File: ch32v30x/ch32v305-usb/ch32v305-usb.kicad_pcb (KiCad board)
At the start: 2 copper layers, 154 x 44 mm, 32 parts, among them J1 USB_C_Receptacle_USB2.0, J2 PGM, J3 RND, J4 JMP-PD, J5 MNT, J6 MNT, J7 MNT, SW1 KEY, SW2 KEY, SW3 KEY, SW4 KEY, SW5 KEY, SW6 KEY, SW7 KEY, SW8 KEY, U1 CH32V305FBP6, U3 3.3vReg, Y1 8MHz12pF

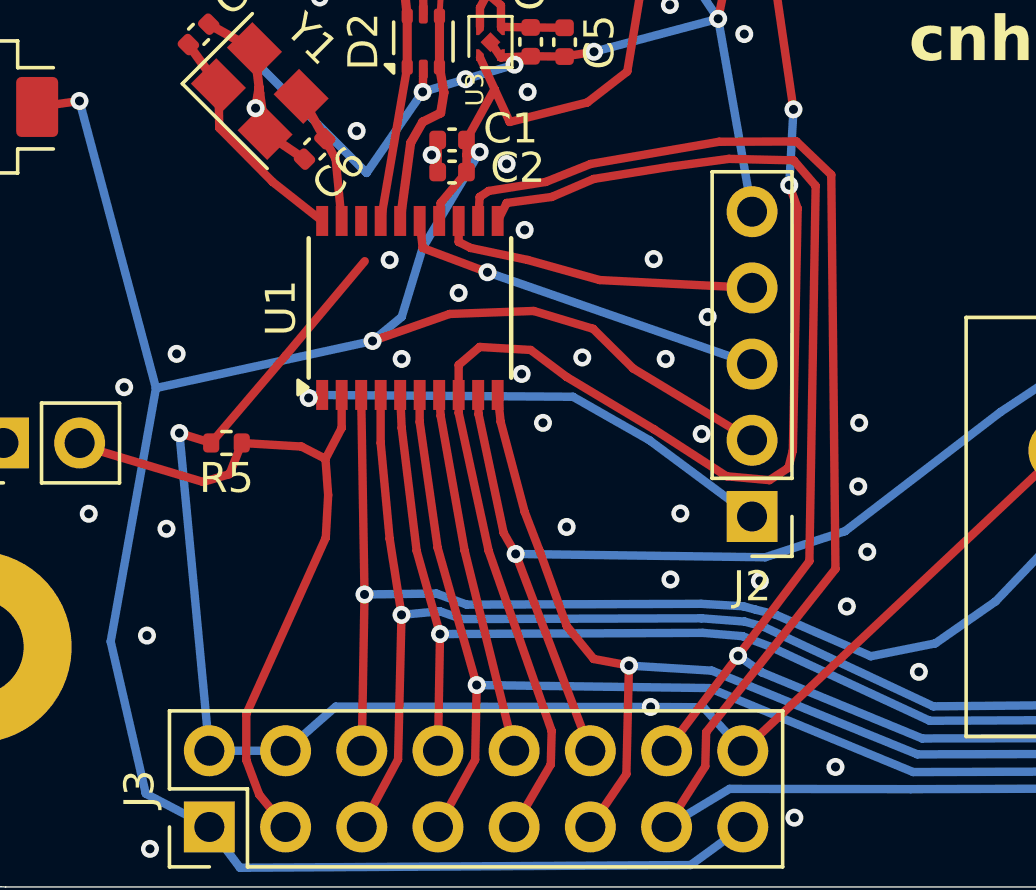
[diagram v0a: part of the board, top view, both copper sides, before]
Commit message: Tweak board to include some pins
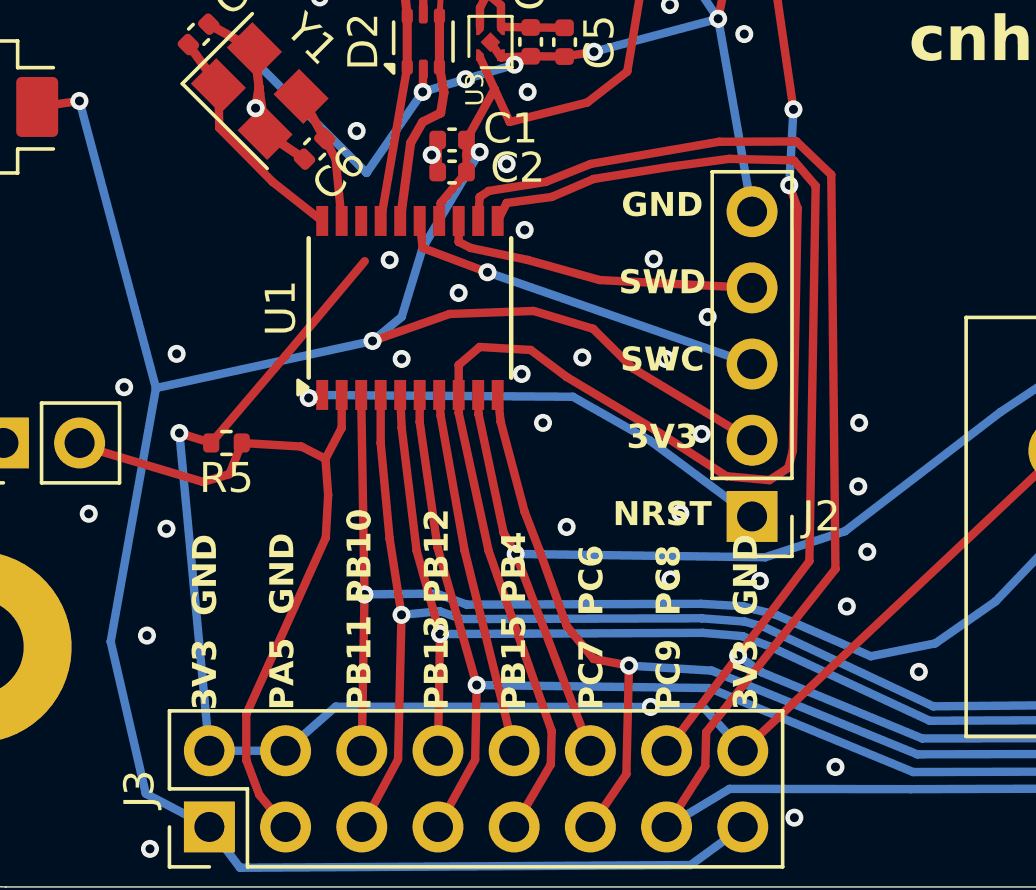
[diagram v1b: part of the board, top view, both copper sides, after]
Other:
- board text added: "3V3 GND PA5 GND PB11 PB10 PB13 PB12 PB15 PB4 PC7 PC6 PC9 PC8 3V3 GND"
- board text added: "GND SWD SWC 3V3 NRST"
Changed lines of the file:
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@@
     (property "ki_keywords" "connector")
     (attr through_hole)
-    (fp_text reference "J2" (at 0 -2.33) (layer "F.SilkS")
+    (fp_text reference "J2" (at -2.316401 -0.003601) (layer "F.SilkS")
         (effects (font (size 1 1) (thickness 0.15)))
     )
@@
   (gr_line (start 63 75) (end 63 103)
     (stroke (width 0.05) (type default)) (layer "Edge.Cuts"))
+  (gr_text "3V3  GND\n\nPA5  GND\n\nPB11 PB10\n\nPB13 PB12\n\nPB15 PB4\n\nPC7  PC6\n\nPC9  PC8\n\n3V3  GND" (at 96.139 105.1052 90) (layer "F.SilkS")
+    (effects (font (size 0.8 0.8) (thickness 0.2) bold) (justify left bottom))
+  )
+  (gr_text "GND\n\nSWD\n\nSWC\n\n3V3\n\nNRST" (at 92.8878 99.0346) (layer "F.SilkS")
+    (effects (font (size 0.8 0.8) (thickness 0.2) bold) (justify bottom))
+  )
   (gr_text "ch32v305-usb\nrev -\ncnhardware" (at 107.97 83.62) (layer "F.SilkS")
     (effects (font (size 1.5 1.5) (thickness 0.3) bold) (justify bottom))
